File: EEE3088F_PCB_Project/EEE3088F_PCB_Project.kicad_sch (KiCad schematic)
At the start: 69 parts, among them IC1 DRV8833PWPR, IC2 DRV8833PWPR, IC3 TPS62067DSGR, IC5 INA219AIDCNR, IC7 TPS61088RHLR, J1 Conn_02x16_Odd_Even, J2 TYPE-C16PIN, J3 Conn_01x02, Q1 AO3400A, Q2 AO3400A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

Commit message: v1.3.1
Most components placed on PCB
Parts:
- L2: footprint (none) -> FHW0805UF2R2JST:L0805
- L4: footprint IND_FXL0420_CMT -> FXL0420-1R2-M KiCADv6:IND_FXL0420_CMT
- LED1: footprint (none) -> KT-0805G:LED0805-R-RD
- LED2: footprint (none) -> KT-0603R:LED0603-RD
- R16, R27, R28, R30: footprint (none) -> R0402:R0402
- R29: footprint (none) -> 0603WAF7502T5E:R0603
- TP1, TP2: footprint (none) -> TestPoint:TestPoint_2Pads_Pitch2.54mm_Drill0.8mm
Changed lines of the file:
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@@
 			)
 		)
-		(property "Footprint" ""
+		(property "Footprint" "KT-0603R:LED0603-RD"
 			(at 198.12 105.41 0)
 			(effects
@@
 			)
 		)
-		(property "Footprint" ""
+		(property "Footprint" "R0402:R0402"
 			(at 236.22 123.19 0)
 			(effects
@@
 			)
 		)
-		(property "Footprint" ""
+		(property "Footprint" "TestPoint:TestPoint_2Pads_Pitch2.54mm_Drill0.8mm"
 			(at 339.09 203.2 0)
 			(effects
@@
 			)
 		)
-		(property "Footprint" ""
+		(property "Footprint" "R0402:R0402"
 			(at 281.94 86.36 0)
 			(effects
@@
 			)
 		)
-		(property "Footprint" ""
+		(property "Footprint" "KT-0805G:LED0805-R-RD"
 			(at 190.5 86.36 0)
 			(effects
@@
 			)
 		)
-		(property "Footprint" "IND_FXL0420_CMT"
+		(property "Footprint" "FXL0420-1R2-M KiCADv6:IND_FXL0420_CMT"
 			(at 360.68 107.95 0)
 			(effects
@@
 			)
 		)
-		(property "Footprint" ""
+		(property "Footprint" "0603WAF7502T5E:R0603"
 			(at 99.06 135.89 0)
 			(effects
@@
 			)
 		)
-		(property "Footprint" ""
+		(property "Footprint" "TestPoint:TestPoint_2Pads_Pitch2.54mm_Drill0.8mm"
 			(at 337.82 246.38 0)
 			(effects
@@
 			)
 		)
-		(property "Footprint" ""
+		(property "Footprint" "R0402:R0402"
 			(at 185.42 67.31 0)
 			(effects
@@
 			)
 		)
-		(property "Footprint" ""
+		(property "Footprint" "FHW0805UF2R2JST:L0805"
 			(at 264.16 74.93 0)
 			(effects
@@
 			)
 		)
-		(property "Footprint" ""
+		(property "Footprint" "R0402:R0402"
 			(at 236.22 109.22 0)
 			(effects

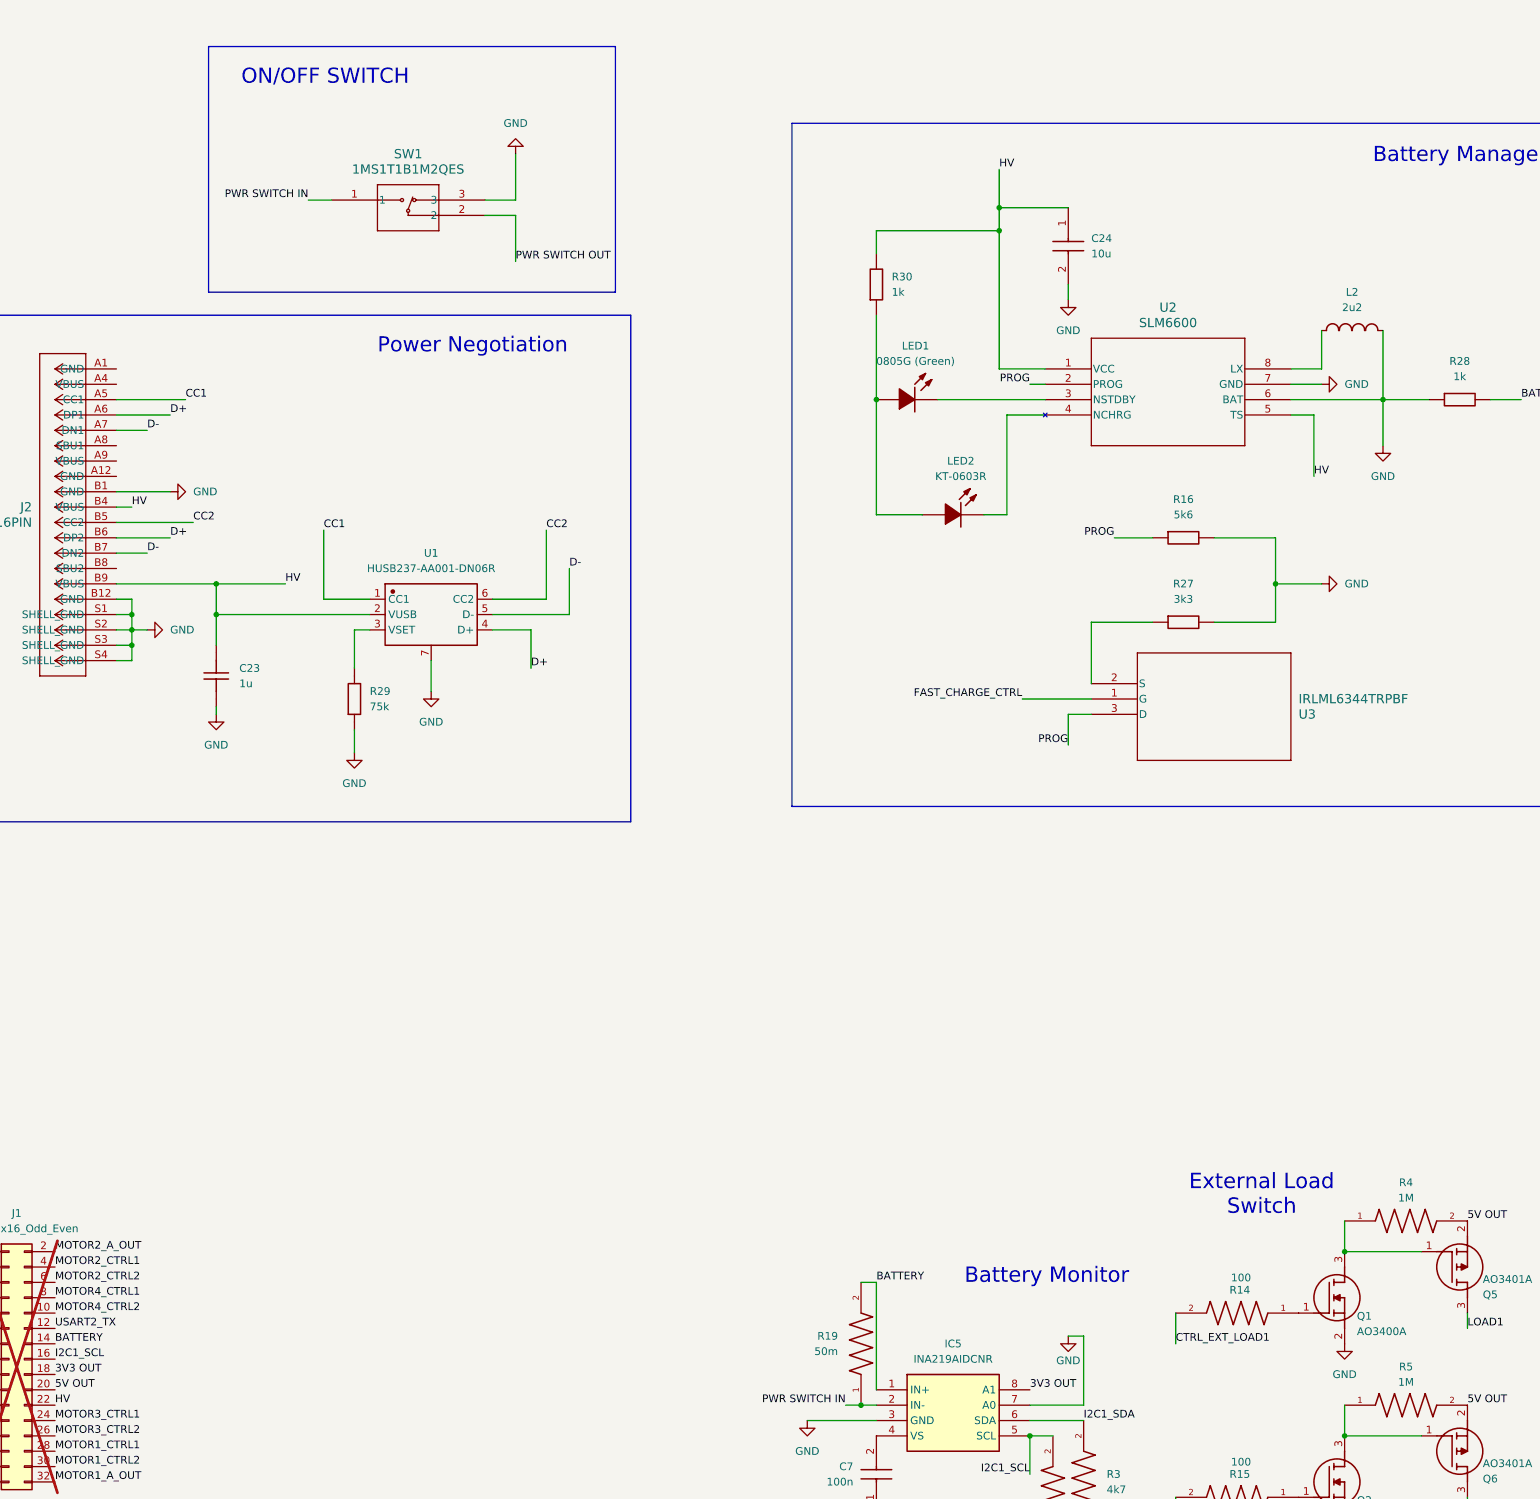
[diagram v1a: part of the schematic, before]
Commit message: v1.3.2
Added test points to my parts of the circuit (and some)
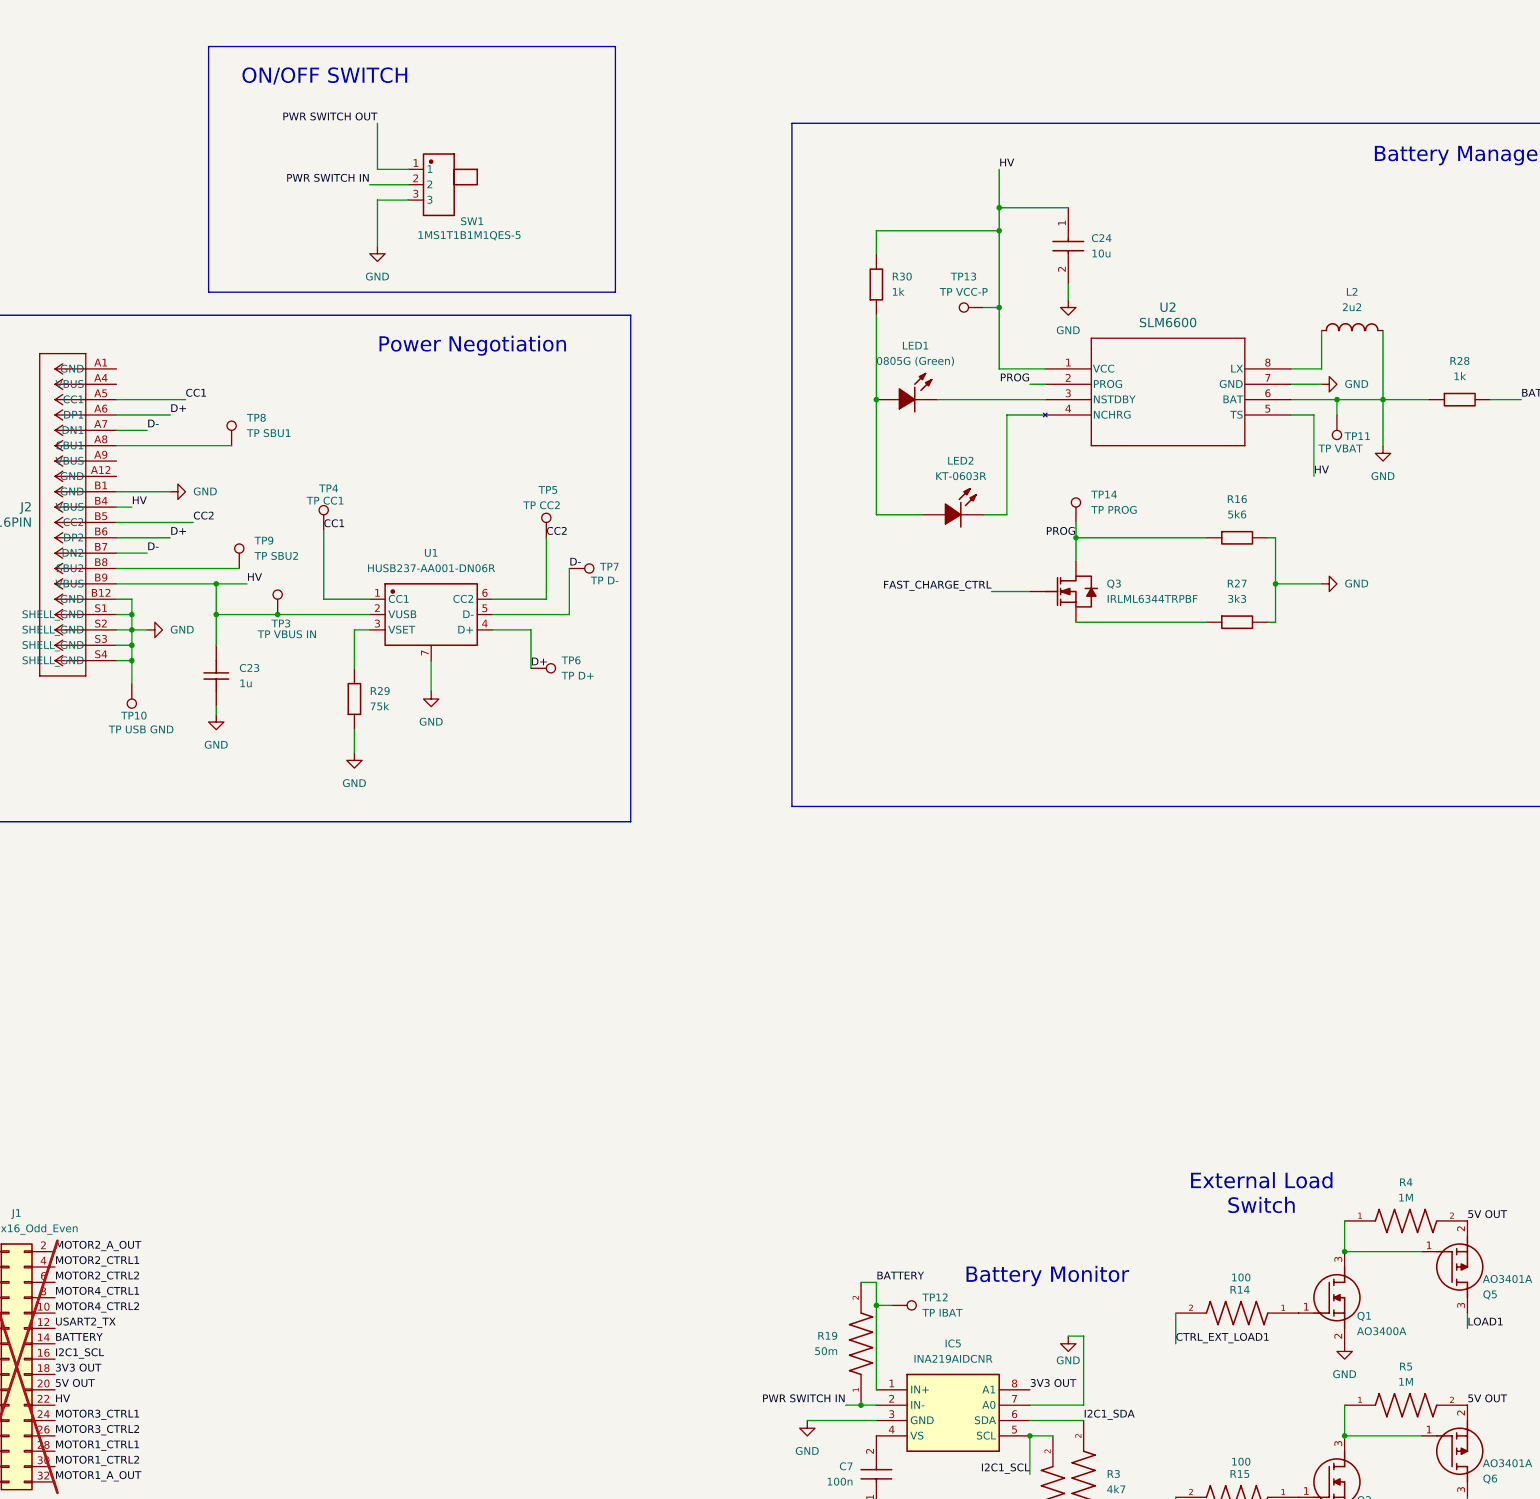
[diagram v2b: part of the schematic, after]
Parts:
- removed SW1: 1MS1T1B1M2QES, 1MS1T1_DYW, symbol 1MS1TIB1M2QES:1MS1T1B1M2QES
- removed U3: IRLML6344TRPBF, IRLML6344TRPBF:IRLML6344TRPBF_INF, symbol IRLML6344TRPBF:IRLML6344TRPBF
- added Q3: IRLML6344TRPBF, symbol IRLML6344TRPBF:IRLML6344TRPBF
- added SW1: 1MS1T1B1M1QES-5, symbol 1MS1TIB1M2QES-5:1MS1T1B1M1QES-5
- added TP10: TP USB GND, symbol Connector:TestPoint
- added TP11: TP VBAT, symbol Connector:TestPoint
- added TP12: TP IBAT, symbol Connector:TestPoint
- added TP13: TP VCC-P, symbol Connector:TestPoint
- added TP14: TP PROG, symbol Connector:TestPoint
- added TP3: TP VBUS IN, symbol Connector:TestPoint
- added TP4: TP CC1, symbol Connector:TestPoint
- added TP5: TP CC2, symbol Connector:TestPoint
- added TP6: TP D+, symbol Connector:TestPoint
- added TP7: TP D-, symbol Connector:TestPoint
- added TP8: TP SBU1, symbol Connector:TestPoint
- added TP9: TP SBU2, symbol Connector:TestPoint
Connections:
- net BATTERY: now also TP12.1
- net CC1: now also TP4.1
- net CC2: now also TP5.1
- net D+: now also TP6.1
- net D-: now also TP7.1
- net FAST_CHARGE_CTRL: now also Q3.1 (G)
- net GND: now also SW1.3, TP10.1, TP11.1
- net HV: now also TP13.1, TP3.1
- net PROG: now also Q3.3 (D), TP14.1
- net PWR SWITCH IN: now also SW1.2
- net PWR SWITCH OUT: now also SW1.1
- net at R27.1: now also Q3.2 (S)
- net at J2.A8 (SBU1): now also TP8.1
- net at J2.B8 (SBU2): now also TP9.1
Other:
- moved on the sheet: R16, R27
